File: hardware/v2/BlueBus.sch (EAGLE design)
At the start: 142 parts, among them J1 3PIN_953442_1, J2 6PIN_953442_1, J3 6PIN_5_103166_1, J4 SJ2-35853A-SMT-TR, J5 SMB_CONN, J6 USB3080-30-01-A, J7 PCM12SMTR, J8 TC2030NL, Q1 NMOSFET-BSS138K, Q2 NMOSFET-BSS138K, Q3 PMOSFET-DMP32D4SSOT323, U1 MPQ4420, U10 PCM5122, U11 PAM8406, U2 TH3122.4, U3 FT231XS, U4 S-1212BC0-U5T1U, U5 XC6210, U6 CAT25M01, U7 PIC24FJ1024GA606, U8 BM83SM1, U9 DIT4096

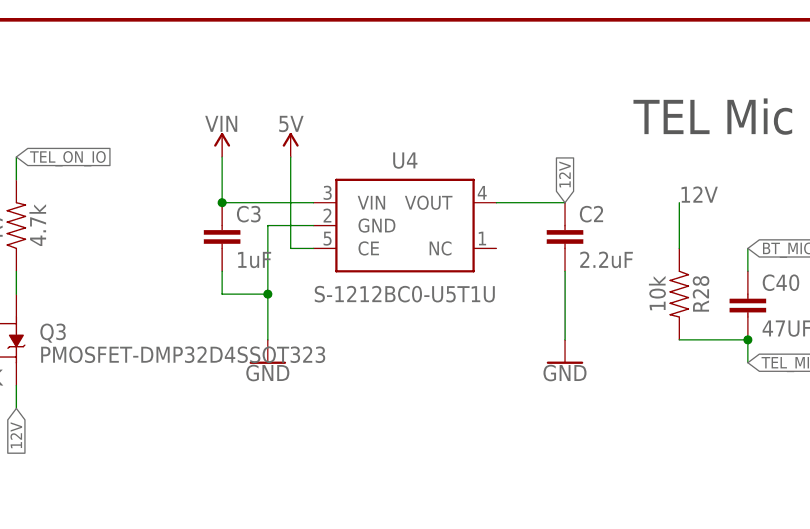
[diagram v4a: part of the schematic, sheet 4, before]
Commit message: [IMP] harcware: Hardware version 2.1 * Swap U4/S-1212BC0 for SOT23-5 package * Update resistor value for R19 to resolve bug with board version identification
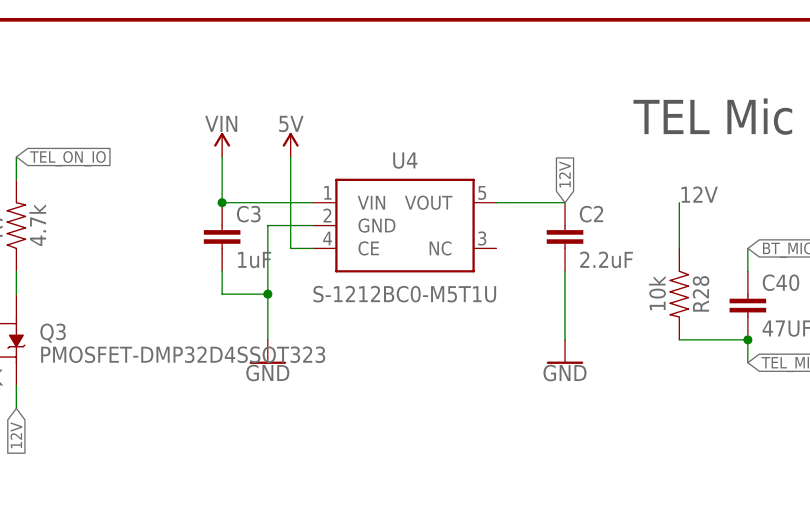
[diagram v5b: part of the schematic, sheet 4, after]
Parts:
- R19: value 10k -> 100; device Passives:10KOHM0603 -> Passives:100OHM0603
- U4: value S-1212BC0-U5T1U -> S-1212BC0-M5T1U; device ICs:S-1212BC0U5T1 -> ICs:S-1212BC0M5T1
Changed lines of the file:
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@@
 <part name="R22" library="Passives" deviceset="20OHM" device="0603" value="20"/>
 <part name="R21" library="Passives" deviceset="20OHM" device="0603" value="20"/>
-<part name="U4" library="ICs" deviceset="S-1212BC0" device="U5T1" value="S-1212BC0-U5T1U"/>
+<part name="U4" library="ICs" deviceset="S-1212BC0" device="M5T1" value="S-1212BC0-M5T1U"/>
 <part name="GND30" library="SparkFun-PowerSymbols" library_urn="urn:adsk.eagle:library:530" deviceset="GND" device=""/>
-<part name="R19" library="Passives" deviceset="10KOHM" device="0603" value="10k"/>
+<part name="R19" library="Passives" deviceset="100OHM" device="0603" value="100"/>
 <part name="R1" library="Passives" deviceset="1KOHM" device="0603" value="1k"/>
 <part name="GND40" library="SparkFun-PowerSymbols" library_urn="urn:adsk.eagle:library:530" deviceset="GND" device=""/>

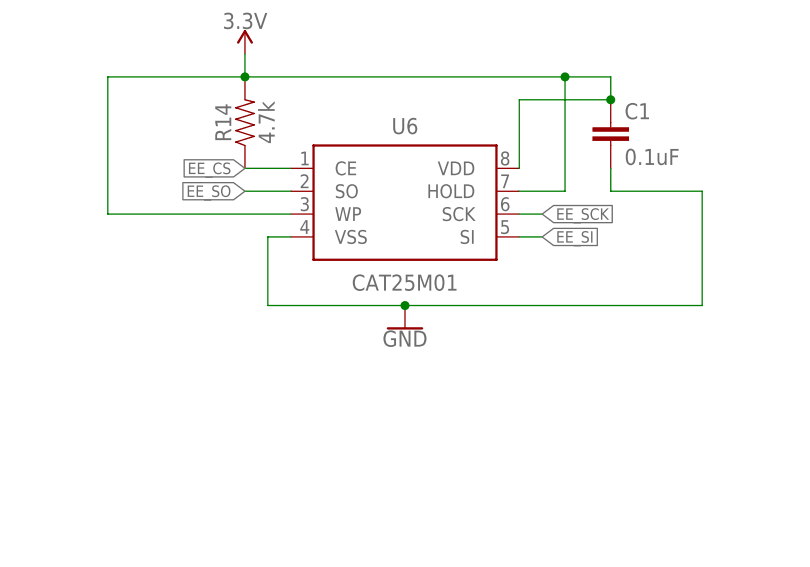
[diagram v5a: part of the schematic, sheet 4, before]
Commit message: [IMP] hardware: Minor updates to v2.1 * Update EEPROM P/N * Update U6 text layer on PCB * Increase USB port locating pin drill size to 0.65mm to prevent PNP issues
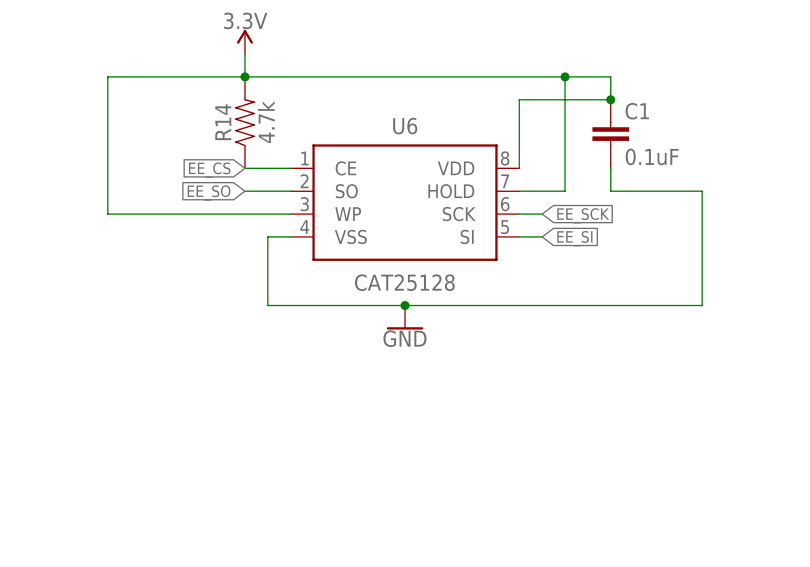
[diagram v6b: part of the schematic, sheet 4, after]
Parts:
- U6: value CAT25M01 -> CAT25128; device ICs:CAT25M01 -> ICs:CAT25128
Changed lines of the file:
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@@
 <part name="U8" library="ICs" deviceset="BM83SM1" device="" value="BM83SM1"/>
 <part name="U9" library="ICs" deviceset="DIT4096" device=""/>
-<part name="U6" library="ICs" deviceset="CAT25M01" device=""/>
+<part name="U6" library="ICs" deviceset="CAT25128" device=""/>
 <part name="C38" library="Passives" deviceset="0.1UF" device="0603" value="0.1uF"/>
 <part name="C37" library="Passives" deviceset="0.1UF" device="0603" value="0.1uF"/>

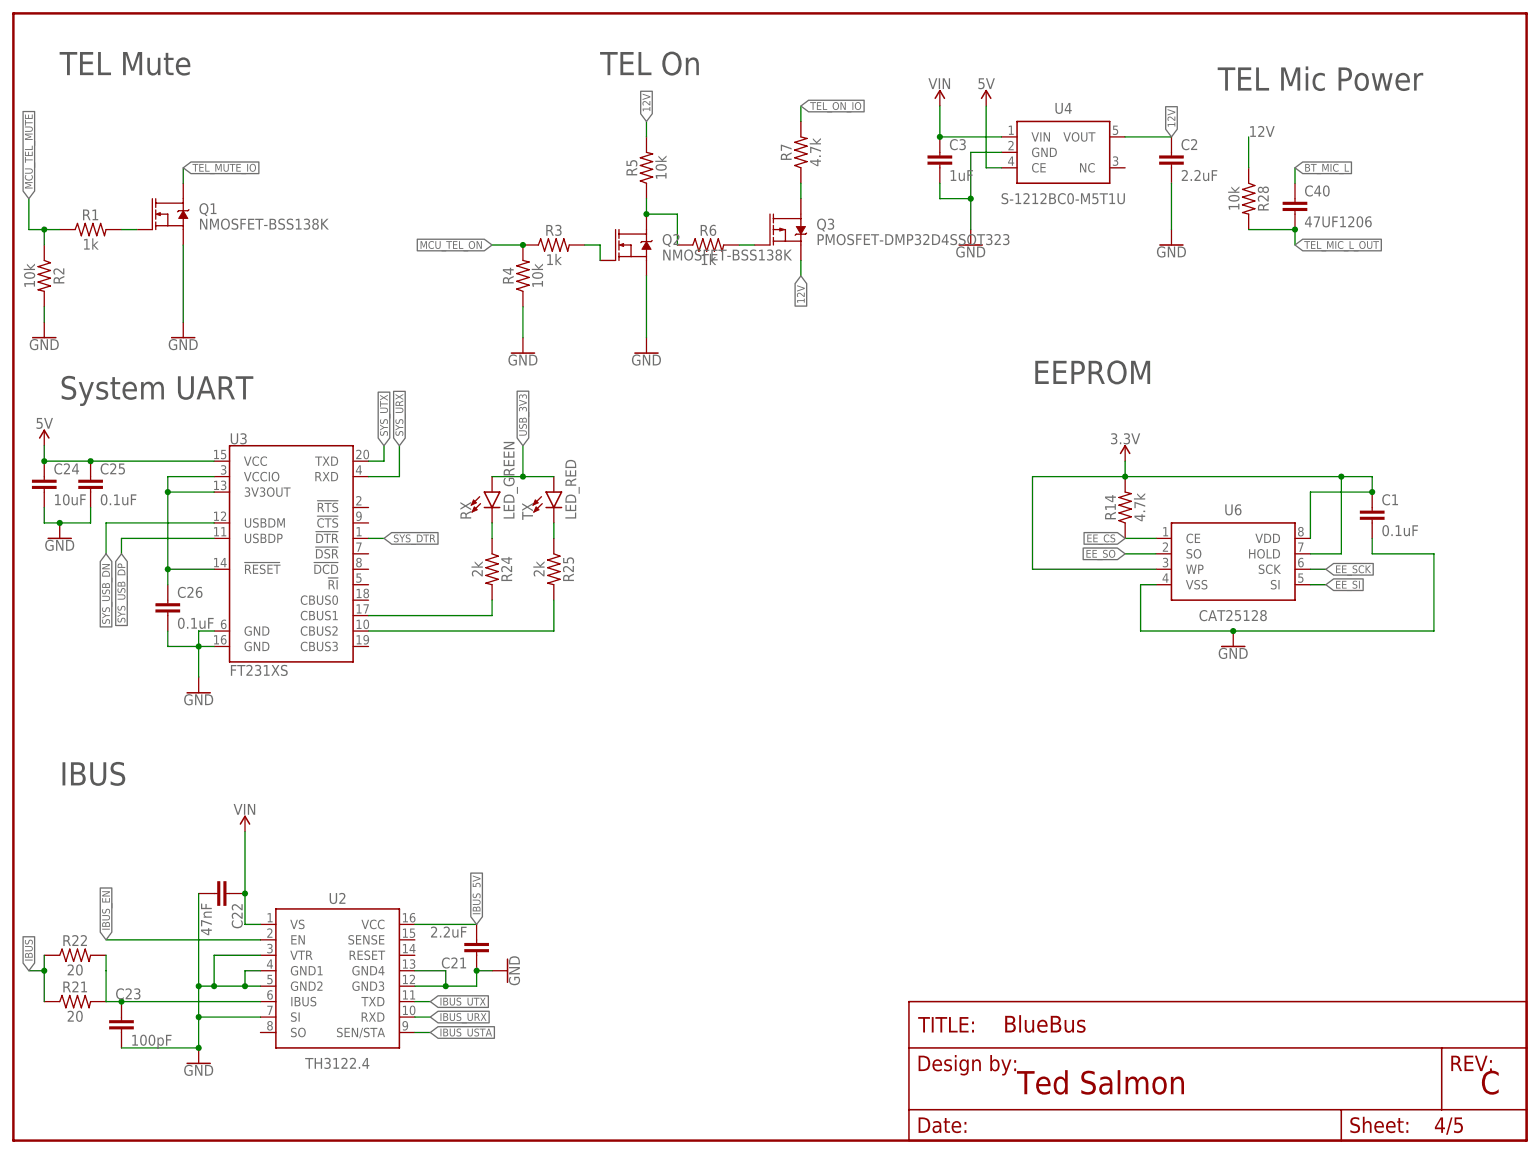
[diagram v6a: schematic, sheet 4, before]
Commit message: [IMP] firmware: Hardware - Version 2.2 * Add 10k pull-up for I/K-Bus * Add switch to make I/K-Bus pull up optional * Switch R7 to 2k ohms
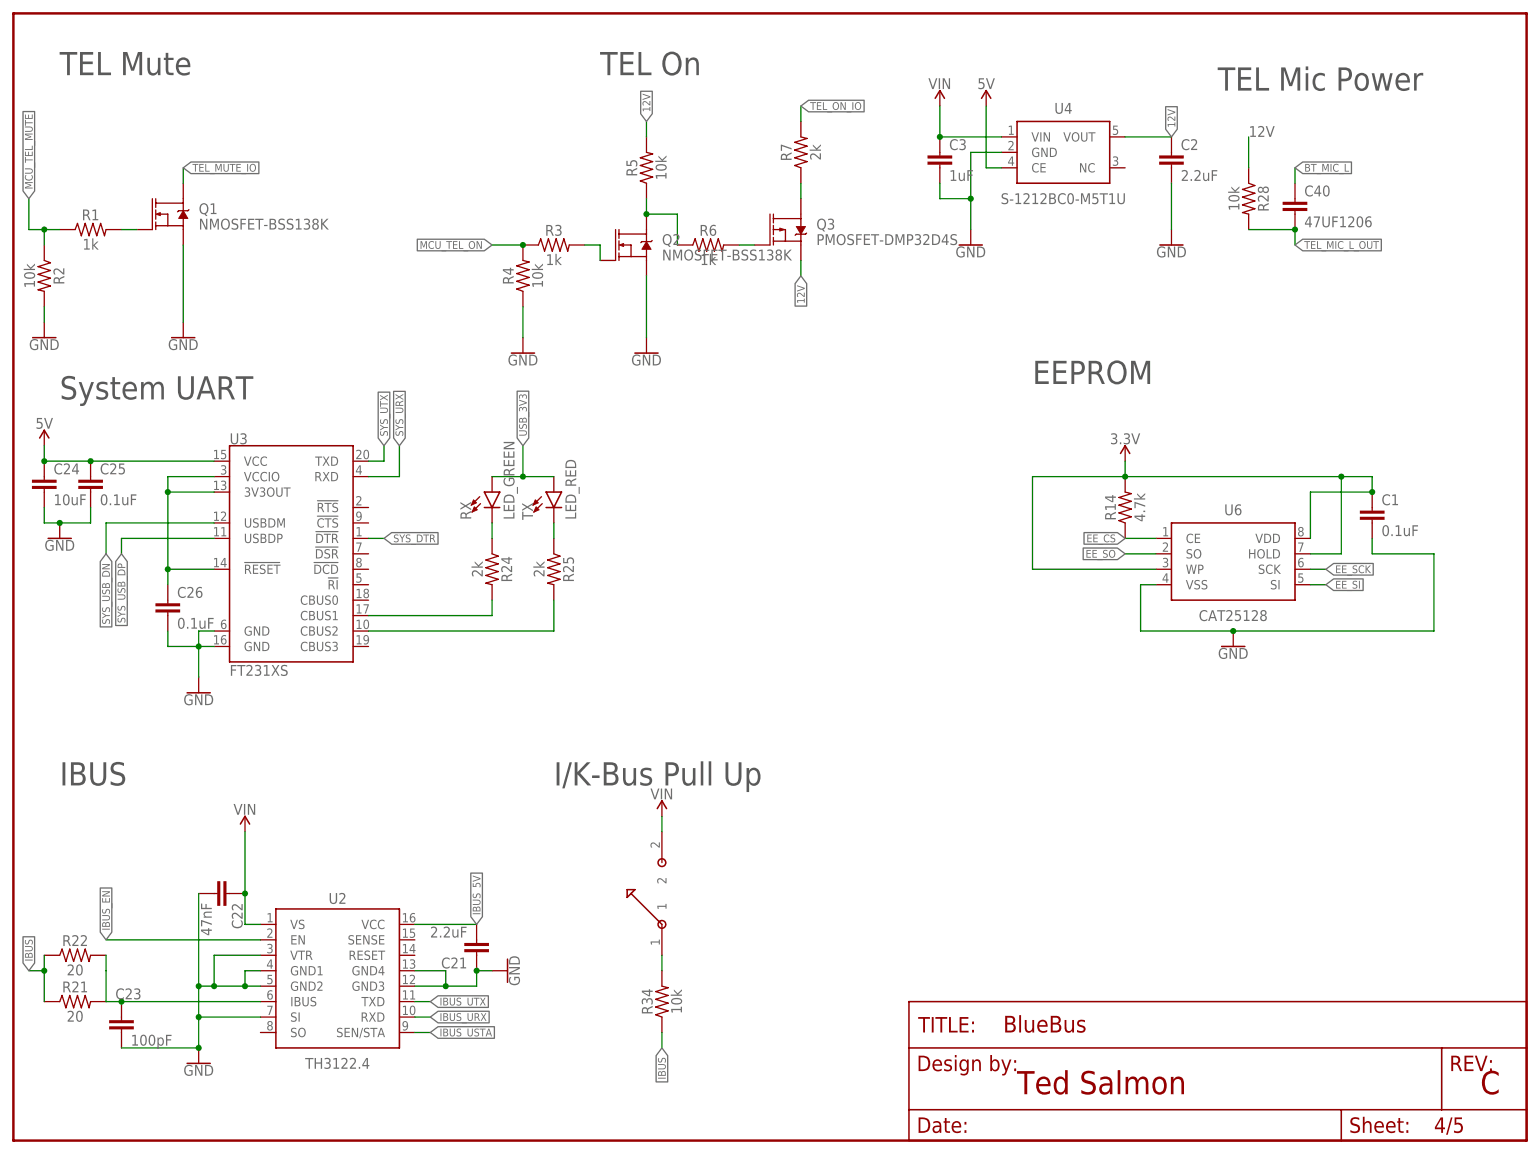
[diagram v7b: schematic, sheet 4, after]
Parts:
- added FB4: 1A/600OHM, Passives:FERRITE_1A/600OHM
- added R34: 10k, Passives:10KOHM0603
- added SW1: CHS-01TA1, Passives:CHS-01TA1
- Q3: value PMOSFET-DMP32D4SSOT323 -> PMOSFET-DMP32D4S; device Passives:PMOSFET-DMP32D4SSOT323 -> Passives:PMOSFET-DMP32D4S
- R7: value 4.7k -> 2k; device Passives:4.7KOHM0603 -> Passives:2KOHM0603
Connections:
- new net DAC_3V3: C50.1, C51.1, C57.1, C58.1, C61.1, C62.1, FB4.2, U10.AVDD, U10.CPVDD, U10.DVDD, U10.MODE2/MS, U10.XSMT
- new net IBUS_PU: R34.2, SW1.1
- net 3.3V: now also FB4.1; no longer C50.1, C51.1, C57.1, C58.1, C61.1, C62.1, U10.AVDD, U10.CPVDD, U10.DVDD, U10.MODE2/MS, U10.XSMT
- net IBUS: now also R34.1
- net VIN: now also SW1.2
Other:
- note added: "Clean up input power"
- note added: "I/K-Bus Pull Up"
